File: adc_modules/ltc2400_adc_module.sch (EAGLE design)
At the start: 4 parts

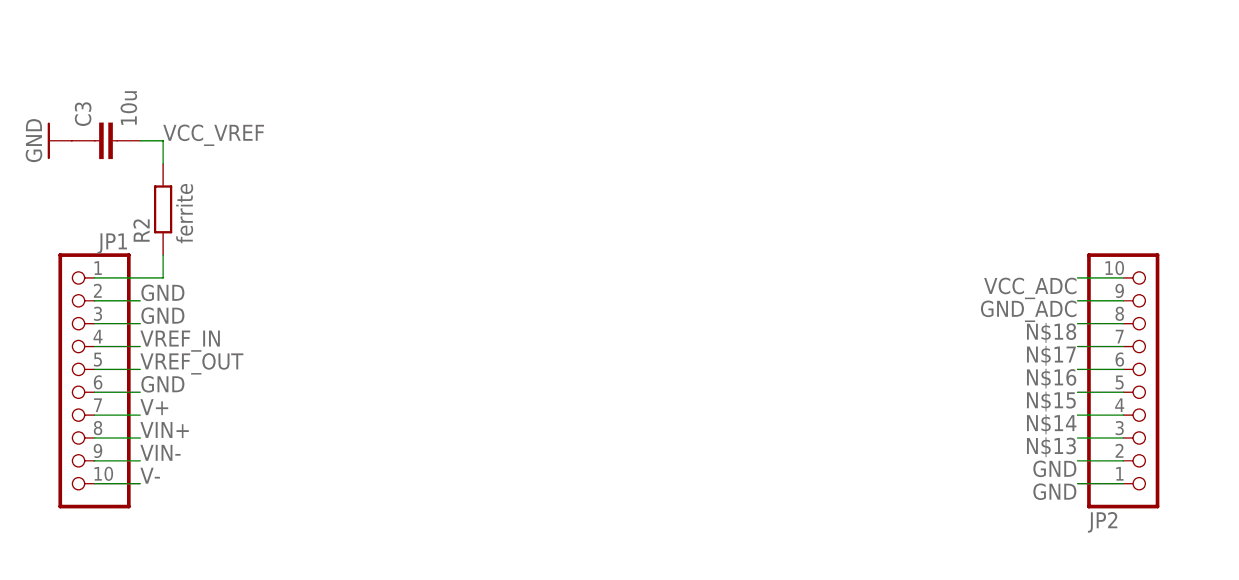
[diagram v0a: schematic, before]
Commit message: * updated and almost finished MCP3551 ADC module
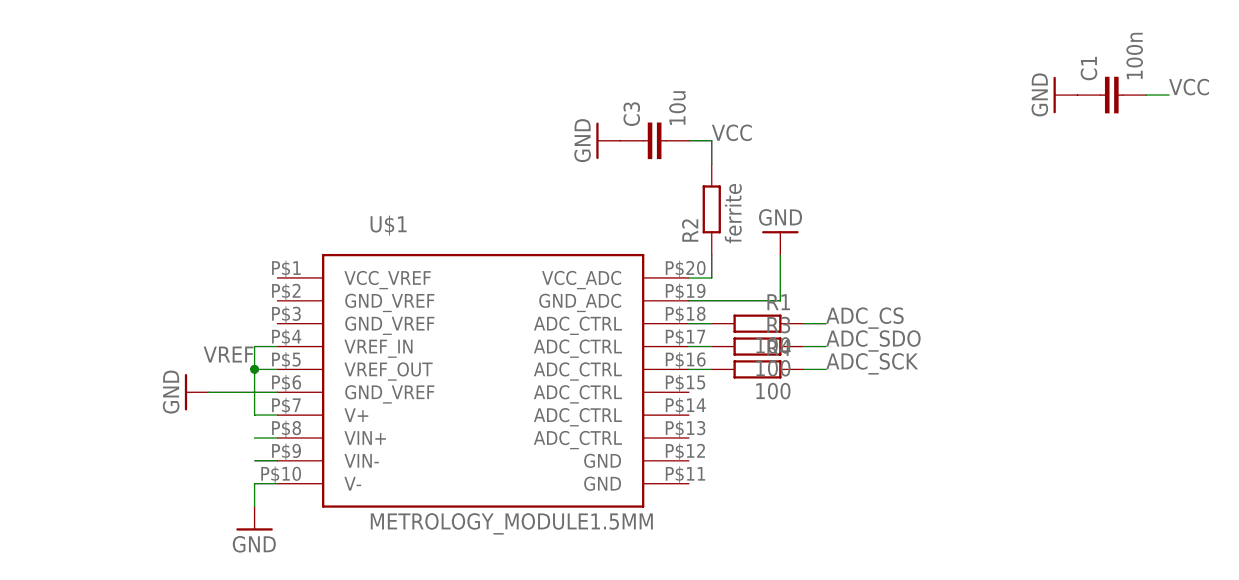
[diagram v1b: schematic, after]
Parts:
- removed JP1, JP2: (no value), SquantorConnectors:PINHD-1X10NORM_OCT
- added C1: 100n, SquantorRCL:C-EUC0603
- added R1, R3, R4: 100, SquantorRCL:R-EU_R0603
- added U$1: METROLOGY_MODULE1.5MM, SquantorPCBOutline:METROLOGY_MODULE1.5MM
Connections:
- removed net GND_ADC: JP2.9
- removed net N$13: JP2.3
- removed net N$14: JP2.4
- removed net N$15: JP2.5
- removed net N$16: JP2.6
- removed net N$17: JP2.7
- removed net N$18: JP2.8
- removed net V+: JP1.7
- removed net V-: JP1.10
- removed net VCC_ADC: JP2.10
- removed net VCC_VREF: C3.2, R2.2
- removed net VIN+: JP1.8
- removed net VIN-: JP1.9
- removed net VREF_IN: JP1.4
- removed net VREF_OUT: JP1.5
- new net ADC_CS: R1.1
- new net ADC_SCK: R4.1
- new net ADC_SDO: R3.1
- new net N$2: R1.2, U$1.ADC_CTRL@18
- new net N$3: R3.2, U$1.ADC_CTRL@17
- new net N$4: R4.2, U$1.ADC_CTRL@16
- new net N$5: U$1.VIN+@8
- new net N$6: U$1.VIN-@9
- new net VCC: C1.2, C3.2, R2.2
- new net VREF: U$1.V+@7, U$1.VREF_IN@4, U$1.VREF_OUT@5
- net GND: now also C1.1, U$1.GND_ADC@19, U$1.GND_VREF@6, U$1.V-@10; no longer JP1.2, JP1.3, JP1.6, JP2.1, JP2.2
- net N$1: now also U$1.VCC_ADC@20; no longer JP1.1
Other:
- moved on the sheet: C3, R2
